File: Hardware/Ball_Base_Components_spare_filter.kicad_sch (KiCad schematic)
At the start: 58 parts, among them J1 Eurorack_10_pin_power, J2 SWD_Header, J3 USB_B_Micro, J4 X_Out, J5 Y_Out, J6 Z_Out, U1 STM32WB35, U3 LD1117-3.3-4Tab, U4 TL072, U5 TL074, Y2 32MHz

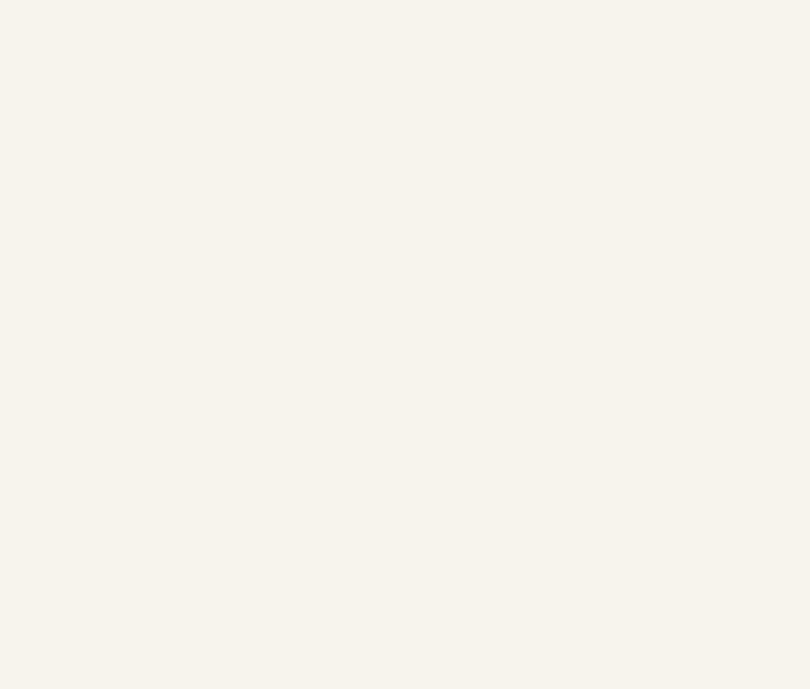
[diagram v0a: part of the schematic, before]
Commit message: First draft of Ball Base pcb completed
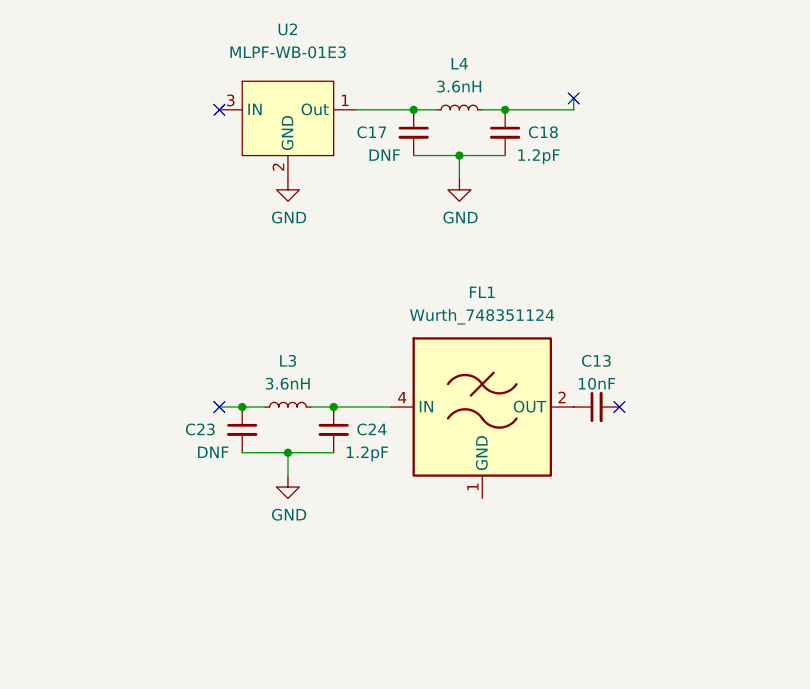
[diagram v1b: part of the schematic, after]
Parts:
- added C13: 10nF, Capacitor_SMD:C_0402_1005Metric, symbol Device:C_Small
- added C17, C23: DNF, Capacitor_SMD:C_0402_1005Metric, symbol Device:C_Small
- added C18, C24: 1.2pF, Capacitor_SMD:C_0402_1005Metric, symbol Device:C_Small
- added FL1: Wurth_748351124, Custom_Footprints:Wurth_2.4GHz_Filter_2.5mm_2.0mm, symbol Wurth_748351124:Wurth_748351124
- added L3, L4: 3.6nH, Inductor_SMD:L_0402_1005Metric, symbol Device:L_Small
- added U2: MLPF-WB-01E3, Custom_Footprints:MLPF-WB-01E3, symbol RF_Filters:MLPF-WB-01E3
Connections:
- net GND: now also C17.2, C18.2, C23.2, C24.2, U2.2 (GND), U2.4 (GND), U2.5 (GND), U2.6 (GND)
- new net: FL1.1 (GND), FL1.3 (GND)
- new net: C13.1, FL1.2 (OUT)
- new net: C24.1, FL1.4 (IN), L3.2
- new net: C18.1, L4.2
- new net: C17.1, L4.1, U2.1 (Out)
- new net: C23.1, L3.1
- no-connect marks 28 -> 32
